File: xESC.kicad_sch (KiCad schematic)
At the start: 16 parts, among them U18 2.54mm 2x2 socket, U21 2.54mm 2x2 socket, U24 2.54mm 2x2 socket, U30 2.54mm 1x6 socket, U33 2.54mm 1x6 socket, U36 2.54mm 1x9 socket, U39 2.54mm 1x5 socket, U8 xESC2

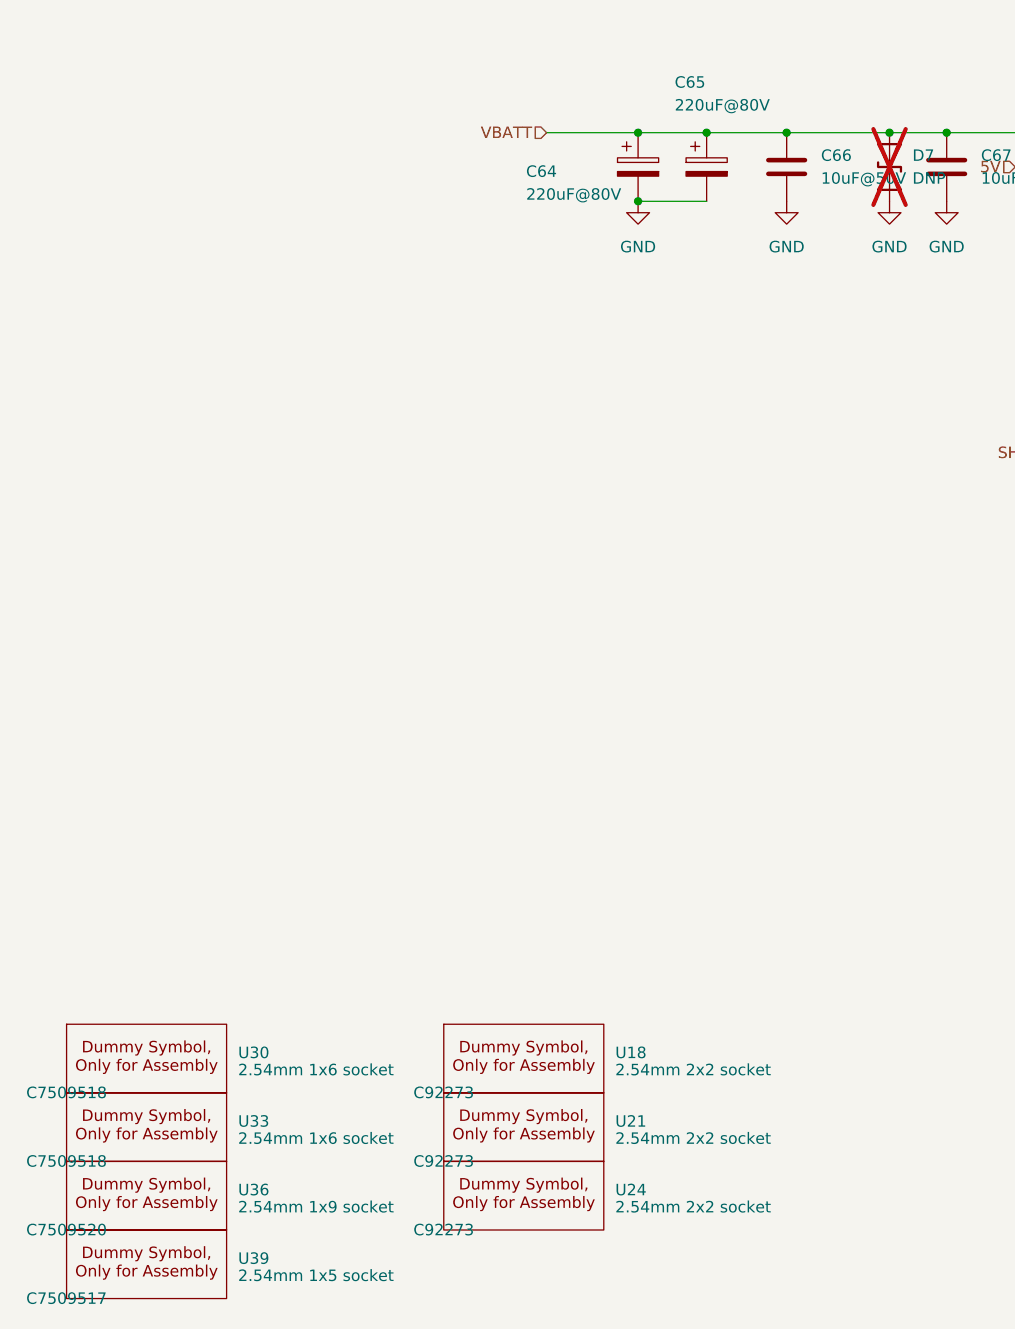
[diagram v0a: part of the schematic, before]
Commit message: Restructured v0.1 for easier worktree use
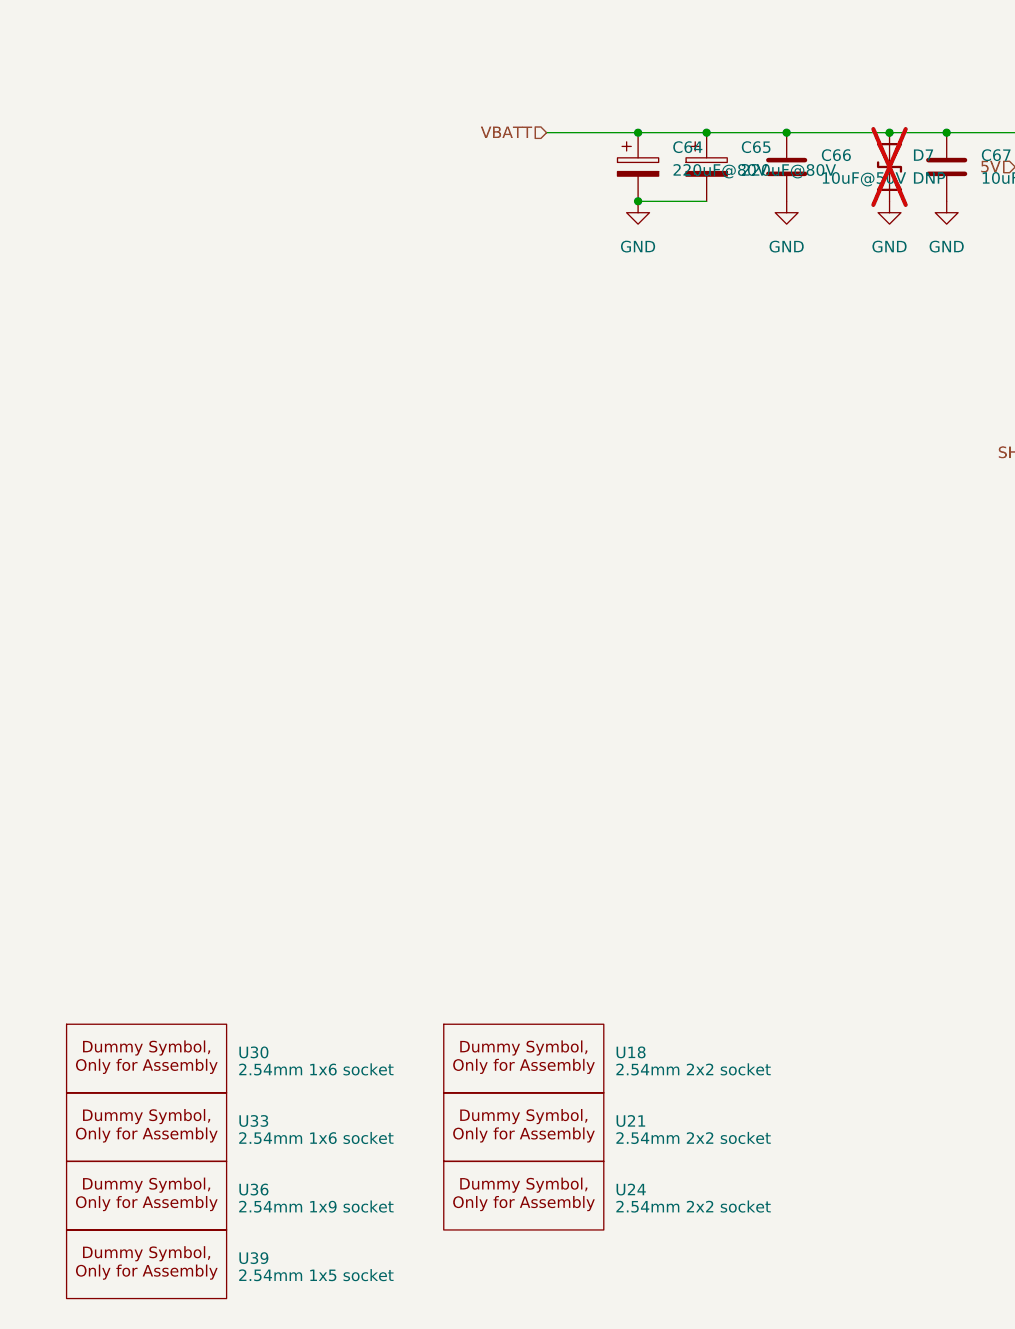
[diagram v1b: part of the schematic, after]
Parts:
- C64, C65: JLC C2937593 -> C106516
- U18, U21, U24: JLC (none) -> C92273; LCSC Part # C92273 -> (none)
- U30, U33: JLC (none) -> C7509518; LCSC Part # C7509518 -> (none)
- U36: JLC (none) -> C7509520; LCSC Part # C7509520 -> (none)
- U39: JLC (none) -> C7509517; LCSC Part # C7509517 -> (none)
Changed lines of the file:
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@@
 	(title_block
 		(title "OpenMower SABO Mainboard for Series I & II")
-		(date "2025-05-22")
-		(rev "v0.2")
+		(date "2025-02-26")
+		(rev "v0.1")
 		(company "Apeheanger <joerg@ebeling.ws> for OpenMower")
 		(comment 1 "This design is licensed under CC BY-NC 4.0")
@@
 			)
 		)
-		(property "JLC" ""
+		(property "JLC" "C7509517"
 			(at 26.67 229.87 0)
 			(effects
@@
 				)
 				(hide yes)
-			)
-		)
-		(property "MPN" ""
-			(at 26.67 229.87 0)
-			(effects
-				(font
-					(size 1.27 1.27)
-				)
-			)
-		)
-		(property "LCSC Part #" "C7509517"
-			(at 26.67 229.87 0)
-			(effects
-				(font
-					(size 1.27 1.27)
-				)
 			)
 		)
@@
 			)
 		)
-		(property "MPN" ""
-			(at 118.11 104.14 0)
-			(effects
-				(font
-					(size 1.27 1.27)
-				)
-			)
-		)
 		(pin "1"
 		)
@@
 			)
 		)
-		(property "MPN" ""
-			(at 166.37 143.51 0)
-			(effects
-				(font
-					(size 1.27 1.27)
-				)
-			)
-		)
 		(pin "14"
 		)
@@
 			)
 		)
-		(property "MPN" ""
-			(at 218.44 113.03 0)
-			(effects
-				(font
-					(size 1.27 1.27)
-				)
-			)
-		)
 		(pin "1"
 		)
@@
 			)
 		)
-		(property "JLC" ""
+		(property "JLC" "C92273"
 			(at 68.58 207.01 0)
 			(effects
@@
 				)
 				(hide yes)
-			)
-		)
-		(property "MPN" ""
-			(at 68.58 207.01 0)
-			(effects
-				(font
-					(size 1.27 1.27)
-				)
-			)
-		)
-		(property "LCSC Part #" "C92273"
-			(at 68.58 207.01 0)
-			(effects
-				(font
-					(size 1.27 1.27)
-				)
 			)
 		)
@@
 			)
 		)
-		(property "MPN" ""
-			(at 124.46 104.14 0)
-			(effects
-				(font
-					(size 1.27 1.27)
-				)
-			)
-		)
 		(pin "1"
 		)
@@
 			)
 		)
-		(property "JLC" ""
+		(property "JLC" "C7509520"
 			(at 26.67 222.25 0)
 			(effects
@@
 				)
 				(hide yes)
-			)
-		)
-		(property "MPN" ""
-			(at 26.67 222.25 0)
-			(effects
-				(font
-					(size 1.27 1.27)
-				)
-			)
-		)
-		(property "LCSC Part #" "C7509520"
-			(at 26.67 222.25 0)
-			(effects
-				(font
-					(size 1.27 1.27)
-				)
 			)
 		)
@@
 			)
 		)
-		(property "JLC" ""
+		(property "JLC" "C7509518"
 			(at 26.67 214.63 0)
 			(effects
@@
 				)
 				(hide yes)
-			)
-		)
-		(property "MPN" ""
-			(at 26.67 214.63 0)
-			(effects
-				(font
-					(size 1.27 1.27)
-				)
-			)
-		)
-		(property "LCSC Part #" "C7509518"
-			(at 26.67 214.63 0)
-			(effects
-				(font
-					(size 1.27 1.27)
-				)
 			)
 		)
@@
 			)
 		)
-		(property "JLC" ""
+		(property "JLC" "C7509518"
 			(at 26.67 207.01 0)
 			(effects
@@
 				)
 				(hide yes)
-			)
-		)
-		(property "MPN" ""
-			(at 26.67 207.01 0)
-			(effects
-				(font
-					(size 1.27 1.27)
-				)
-			)
-		)
-		(property "LCSC Part #" "C7509518"
-			(at 26.67 207.01 0)
-			(effects
-				(font
-					(size 1.27 1.27)
-				)
 			)
 		)
@@
 			)
 		)
-		(property "JLC" ""
+		(property "JLC" "C92273"
 			(at 68.58 214.63 0)
 			(effects
@@
 				)
 				(hide yes)
-			)
-		)
-		(property "MPN" ""
-			(at 68.58 214.63 0)
-			(effects
-				(font
-					(size 1.27 1.27)
-				)
-			)
-		)
-		(property "LCSC Part #" "C92273"
-			(at 68.58 214.63 0)
-			(effects
-				(font
-					(size 1.27 1.27)
-				)
 			)
 		)
@@
 		(on_board yes)
 		(dnp no)
+		(fields_autoplaced yes)
 		(property "Reference" "C64"
-			(at 77.724 104.648 0)
+			(at 93.98 101.9809 0)
 			(effects
 				(font
@@
 		)
 		(property "Value" "220uF@80V"
-			(at 77.724 107.188 0)
+			(at 93.98 104.5209 0)
 			(effects
 				(font
@@
 			)
 		)
-		(property "Description" "220uF 80V Plugin,D10xL16mm  Aluminum Electrolytic Capacitors - Leaded ROHS"
+		(property "Description" "Polarized capacitor"
 			(at 90.17 104.14 0)
 			(effects
@@
 			)
 		)
-		(property "JLC" "C2937593 "
+		(property "JLC" "C106516"
 			(at 90.17 104.14 0)
 			(effects
@@
 				)
 				(hide yes)
-			)
-		)
-		(property "MPN" ""
-			(at 90.17 104.14 0)
-			(effects
-				(font
-					(size 1.27 1.27)
-				)
 			)
 		)
@@
 			)
 		)
-		(property "MPN" ""
-			(at 199.39 113.03 0)
-			(effects
-				(font
-					(size 1.27 1.27)
-				)
-			)
-		)
 		(pin "1"
 		)
@@
 			)
 		)
-		(property "MPN" ""
-			(at 106.68 104.14 0)
-			(effects
-				(font
-					(size 1.27 1.27)
-				)
-			)
-		)
 		(pin "1"
 		)
@@
 		(on_board yes)
 		(dnp no)
+		(fields_autoplaced yes)
 		(property "Reference" "C65"
-			(at 94.234 94.742 0)
+			(at 101.6 101.9809 0)
 			(effects
 				(font
@@
 		)
 		(property "Value" "220uF@80V"
-			(at 94.234 97.282 0)
+			(at 101.6 104.5209 0)
 			(effects
 				(font
@@
 			)
 		)
-		(property "Description" "220uF 80V Plugin,D10xL16mm  Aluminum Electrolytic Capacitors - Leaded ROHS"
+		(property "Description" "Polarized capacitor"
 			(at 97.79 104.14 0)
 			(effects
@@
 			)
 		)
-		(property "JLC" "C2937593 "
+		(property "JLC" "C106516"
 			(at 97.79 104.14 0)
 			(effects
@@
 				)
 				(hide yes)
-			)
-		)
-		(property "MPN" ""
-			(at 97.79 104.14 0)
-			(effects
-				(font
-					(size 1.27 1.27)
-				)
 			)
 		)
@@
 			)
 		)
-		(property "JLC" ""
+		(property "JLC" "C92273"
 			(at 68.58 222.25 0)
 			(effects
@@
 				)
 				(hide yes)
-			)
-		)
-		(property "MPN" ""
-			(at 68.58 222.25 0)
-			(effects
-				(font
-					(size 1.27 1.27)
-				)
-			)
-		)
-		(property "LCSC Part #" "C92273"
-			(at 68.58 222.25 0)
-			(effects
-				(font
-					(size 1.27 1.27)
-				)
 			)
 		)
@@
 			)
 		)
-		(property "MPN" ""
-			(at 209.55 113.03 0)
-			(effects
-				(font
-					(size 1.27 1.27)
-				)
-			)
-		)

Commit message: Prepare v0.2
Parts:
- C64, C65: JLC C106516 -> C2937593
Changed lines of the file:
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@@
 	(title_block
 		(title "OpenMower SABO Mainboard for Series I & II")
-		(date "2025-02-26")
-		(rev "v0.1")
+		(date "2025-05-04")
+		(rev "v0.2")
 		(company "Apeheanger <joerg@ebeling.ws> for OpenMower")
 		(comment 1 "This design is licensed under CC BY-NC 4.0")
@@
 		(on_board yes)
 		(dnp no)
-		(fields_autoplaced yes)
 		(property "Reference" "C64"
-			(at 93.98 101.9809 0)
+			(at 77.724 104.648 0)
 			(effects
 				(font
@@
 		)
 		(property "Value" "220uF@80V"
-			(at 93.98 104.5209 0)
+			(at 77.724 107.188 0)
 			(effects
 				(font
@@
 			)
 		)
-		(property "Description" "Polarized capacitor"
+		(property "Description" "220uF 80V Plugin,D10xL16mm  Aluminum Electrolytic Capacitors - Leaded ROHS"
 			(at 90.17 104.14 0)
 			(effects
@@
 			)
 		)
-		(property "JLC" "C106516"
+		(property "JLC" "C2937593 "
 			(at 90.17 104.14 0)
 			(effects
@@
 		(on_board yes)
 		(dnp no)
-		(fields_autoplaced yes)
 		(property "Reference" "C65"
-			(at 101.6 101.9809 0)
+			(at 94.234 94.742 0)
 			(effects
 				(font
@@
 		)
 		(property "Value" "220uF@80V"
-			(at 101.6 104.5209 0)
+			(at 94.234 97.282 0)
 			(effects
 				(font
@@
 			)
 		)
-		(property "Description" "Polarized capacitor"
+		(property "Description" "220uF 80V Plugin,D10xL16mm  Aluminum Electrolytic Capacitors - Leaded ROHS"
 			(at 97.79 104.14 0)
 			(effects
@@
 			)
 		)
-		(property "JLC" "C106516"
+		(property "JLC" "C2937593 "
 			(at 97.79 104.14 0)
 			(effects

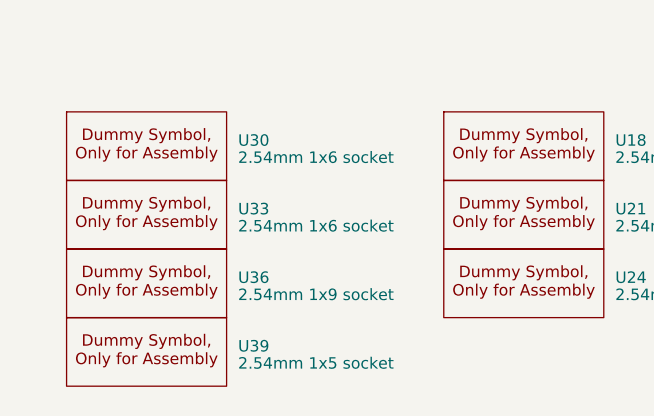
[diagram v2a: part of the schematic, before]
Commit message: Add RoHS Compliance Summary
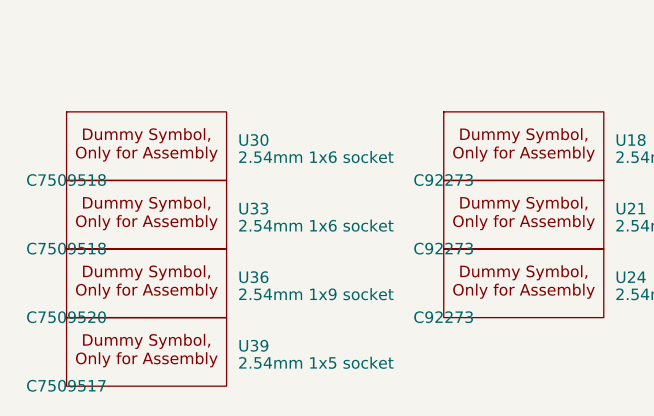
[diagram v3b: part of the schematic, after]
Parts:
- U18, U21, U24: JLC C92273 -> (none); LCSC Part # (none) -> C92273
- U30, U33: JLC C7509518 -> (none); LCSC Part # (none) -> C7509518
- U36: JLC C7509520 -> (none); LCSC Part # (none) -> C7509520
- U39: JLC C7509517 -> (none); LCSC Part # (none) -> C7509517
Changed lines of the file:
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@@
 			)
 		)
-		(property "JLC" "C7509517"
+		(property "JLC" ""
 			(at 26.67 229.87 0)
 			(effects
@@
 				)
 				(hide yes)
+			)
+		)
+		(property "MPN" ""
+			(at 26.67 229.87 0)
+			(effects
+				(font
+					(size 1.27 1.27)
+				)
+			)
+		)
+		(property "LCSC Part #" "C7509517"
+			(at 26.67 229.87 0)
+			(effects
+				(font
+					(size 1.27 1.27)
+				)
 			)
 		)
@@
 			)
 		)
+		(property "MPN" ""
+			(at 118.11 104.14 0)
+			(effects
+				(font
+					(size 1.27 1.27)
+				)
+			)
+		)
 		(pin "1"
 		)
@@
 			)
 		)
+		(property "MPN" ""
+			(at 166.37 143.51 0)
+			(effects
+				(font
+					(size 1.27 1.27)
+				)
+			)
+		)
 		(pin "14"
 		)
@@
 			)
 		)
+		(property "MPN" ""
+			(at 218.44 113.03 0)
+			(effects
+				(font
+					(size 1.27 1.27)
+				)
+			)
+		)
 		(pin "1"
 		)
@@
 			)
 		)
-		(property "JLC" "C92273"
+		(property "JLC" ""
 			(at 68.58 207.01 0)
 			(effects
@@
 				)
 				(hide yes)
+			)
+		)
+		(property "MPN" ""
+			(at 68.58 207.01 0)
+			(effects
+				(font
+					(size 1.27 1.27)
+				)
+			)
+		)
+		(property "LCSC Part #" "C92273"
+			(at 68.58 207.01 0)
+			(effects
+				(font
+					(size 1.27 1.27)
+				)
 			)
 		)
@@
 			)
 		)
+		(property "MPN" ""
+			(at 124.46 104.14 0)
+			(effects
+				(font
+					(size 1.27 1.27)
+				)
+			)
+		)
 		(pin "1"
 		)
@@
 			)
 		)
-		(property "JLC" "C7509520"
+		(property "JLC" ""
 			(at 26.67 222.25 0)
 			(effects
@@
 				)
 				(hide yes)
+			)
+		)
+		(property "MPN" ""
+			(at 26.67 222.25 0)
+			(effects
+				(font
+					(size 1.27 1.27)
+				)
+			)
+		)
+		(property "LCSC Part #" "C7509520"
+			(at 26.67 222.25 0)
+			(effects
+				(font
+					(size 1.27 1.27)
+				)
 			)
 		)
@@
 			)
 		)
-		(property "JLC" "C7509518"
+		(property "JLC" ""
 			(at 26.67 214.63 0)
 			(effects
@@
 				)
 				(hide yes)
+			)
+		)
+		(property "MPN" ""
+			(at 26.67 214.63 0)
+			(effects
+				(font
+					(size 1.27 1.27)
+				)
+			)
+		)
+		(property "LCSC Part #" "C7509518"
+			(at 26.67 214.63 0)
+			(effects
+				(font
+					(size 1.27 1.27)
+				)
 			)
 		)
@@
 			)
 		)
-		(property "JLC" "C7509518"
+		(property "JLC" ""
 			(at 26.67 207.01 0)
 			(effects
@@
 				)
 				(hide yes)
+			)
+		)
+		(property "MPN" ""
+			(at 26.67 207.01 0)
+			(effects
+				(font
+					(size 1.27 1.27)
+				)
+			)
+		)
+		(property "LCSC Part #" "C7509518"
+			(at 26.67 207.01 0)
+			(effects
+				(font
+					(size 1.27 1.27)
+				)
 			)
 		)
@@
 			)
 		)
-		(property "JLC" "C92273"
+		(property "JLC" ""
 			(at 68.58 214.63 0)
 			(effects
@@
 				)
 				(hide yes)
+			)
+		)
+		(property "MPN" ""
+			(at 68.58 214.63 0)
+			(effects
+				(font
+					(size 1.27 1.27)
+				)
+			)
+		)
+		(property "LCSC Part #" "C92273"
+			(at 68.58 214.63 0)
+			(effects
+				(font
+					(size 1.27 1.27)
+				)
 			)
 		)
@@
 			)
 		)
+		(property "MPN" ""
+			(at 90.17 104.14 0)
+			(effects
+				(font
+					(size 1.27 1.27)
+				)
+			)
+		)
 		(pin "1"
 		)
@@
 			)
 		)
+		(property "MPN" ""
+			(at 199.39 113.03 0)
+			(effects
+				(font
+					(size 1.27 1.27)
+				)
+			)
+		)
 		(pin "1"
 		)
@@
 			)
 		)
+		(property "MPN" ""
+			(at 106.68 104.14 0)
+			(effects
+				(font
+					(size 1.27 1.27)
+				)
+			)
+		)
 		(pin "1"
 		)
@@
 				)
 				(hide yes)
+			)
+		)
+		(property "MPN" ""
+			(at 97.79 104.14 0)
+			(effects
+				(font
+					(size 1.27 1.27)
+				)
 			)
 		)
@@
 			)
 		)
-		(property "JLC" "C92273"
+		(property "JLC" ""
 			(at 68.58 222.25 0)
 			(effects
@@
 				)
 				(hide yes)
+			)
+		)
+		(property "MPN" ""
+			(at 68.58 222.25 0)
+			(effects
+				(font
+					(size 1.27 1.27)
+				)
+			)
+		)
+		(property "LCSC Part #" "C92273"
+			(at 68.58 222.25 0)
+			(effects
+				(font
+					(size 1.27 1.27)
+				)
 			)
 		)
@@
 			)
 		)
+		(property "MPN" ""
+			(at 209.55 113.03 0)
+			(effects
+				(font
+					(size 1.27 1.27)
+				)
+			)
+		)
